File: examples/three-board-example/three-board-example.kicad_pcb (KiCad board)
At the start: 6 copper layers, 55 x 50 mm, 3 parts, among them U1 LM555xM, U2 LM555xM

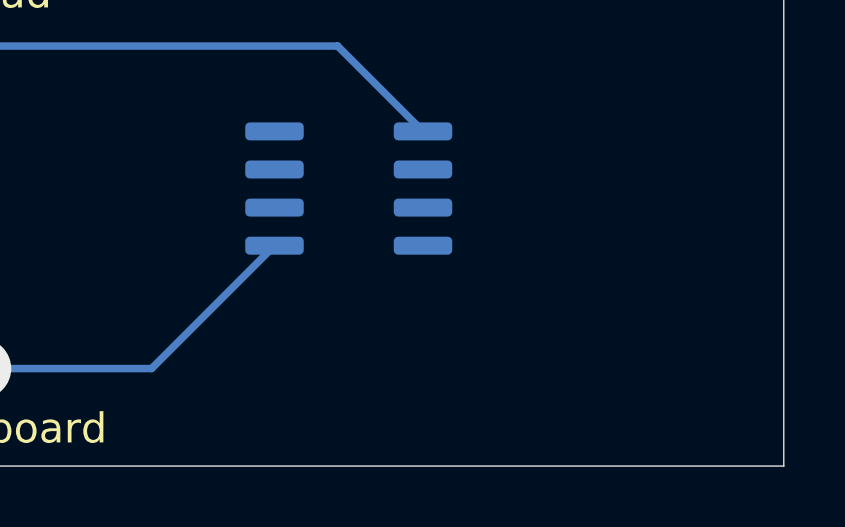
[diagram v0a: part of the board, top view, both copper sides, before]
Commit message: tracks working, and buried vias working
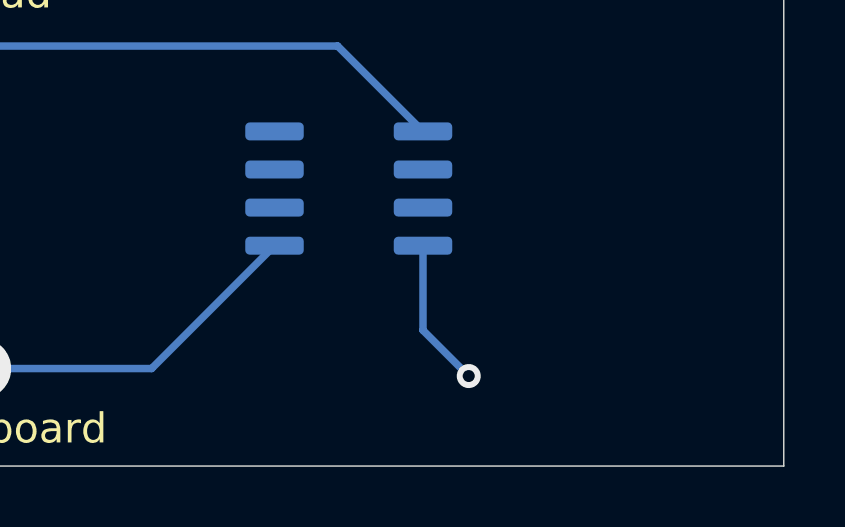
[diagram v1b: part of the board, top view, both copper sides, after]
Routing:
- net Net-(U2-Pad8): track 0.00 -> 9.73 mm, vias 0 -> 1

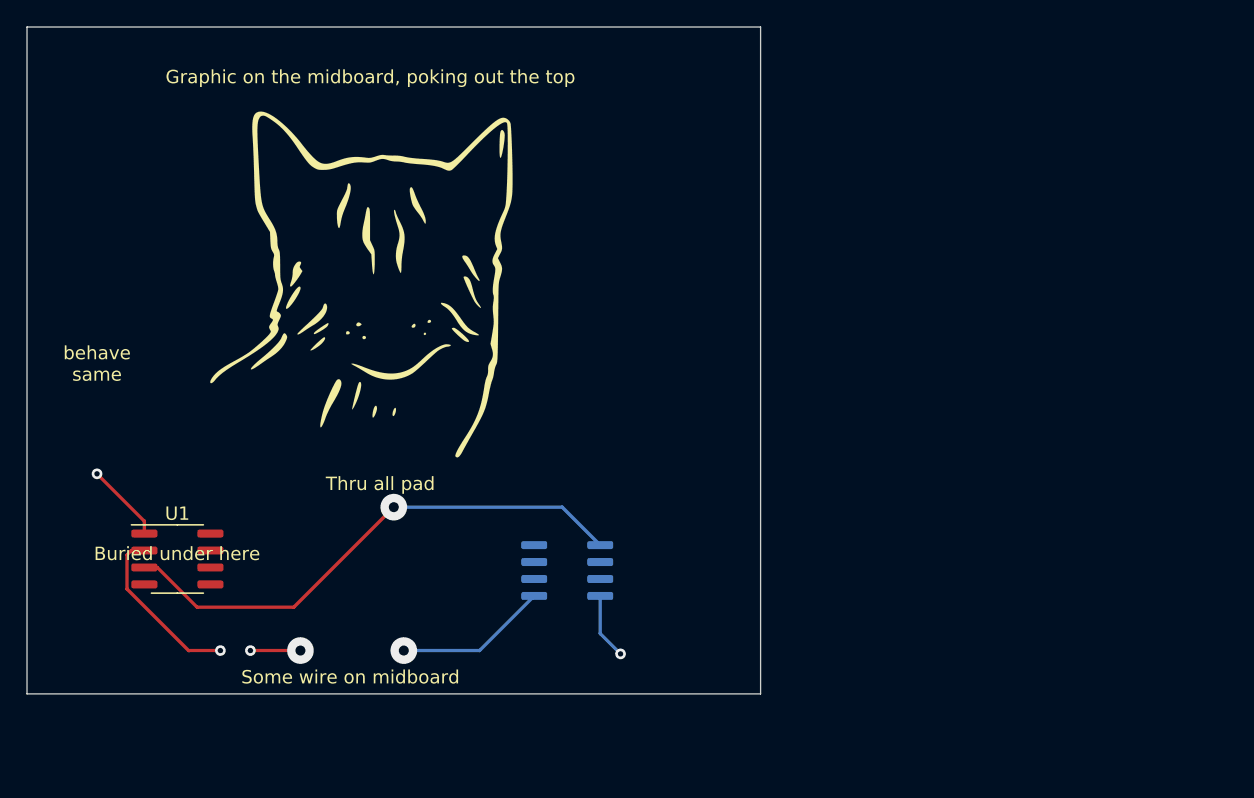
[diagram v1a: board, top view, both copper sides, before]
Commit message: vias and bond pads working. checked with inside and outside styles
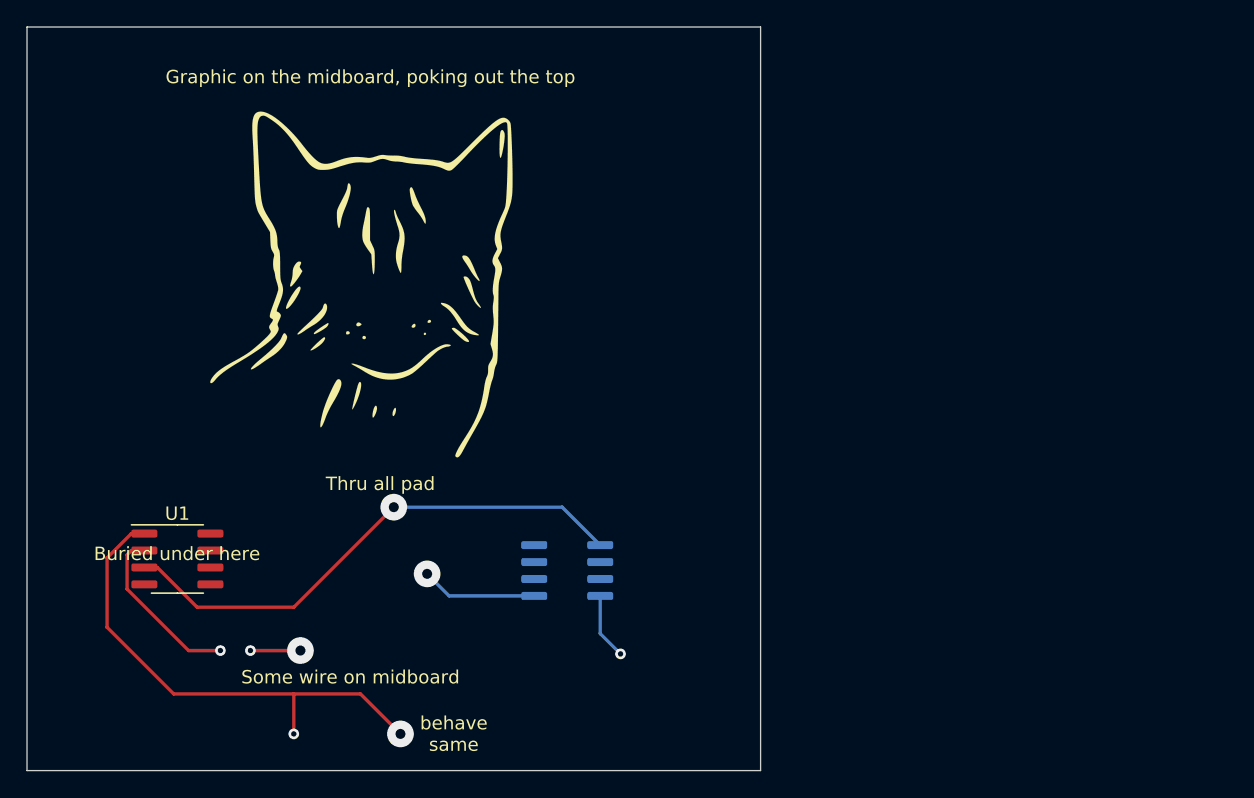
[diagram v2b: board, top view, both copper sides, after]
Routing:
- net Net-(U1-Pad1): track 14.5 -> 49.1 mm, vias 2 -> 4
- net Net-(U1-Pad2): track 38.1 -> 40.7 mm
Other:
- board size 55 x 50 mm -> 55 x 55.8 mm

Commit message: Special modules for cutting, meaning that the drawings from within the modules are exploded to cut layers
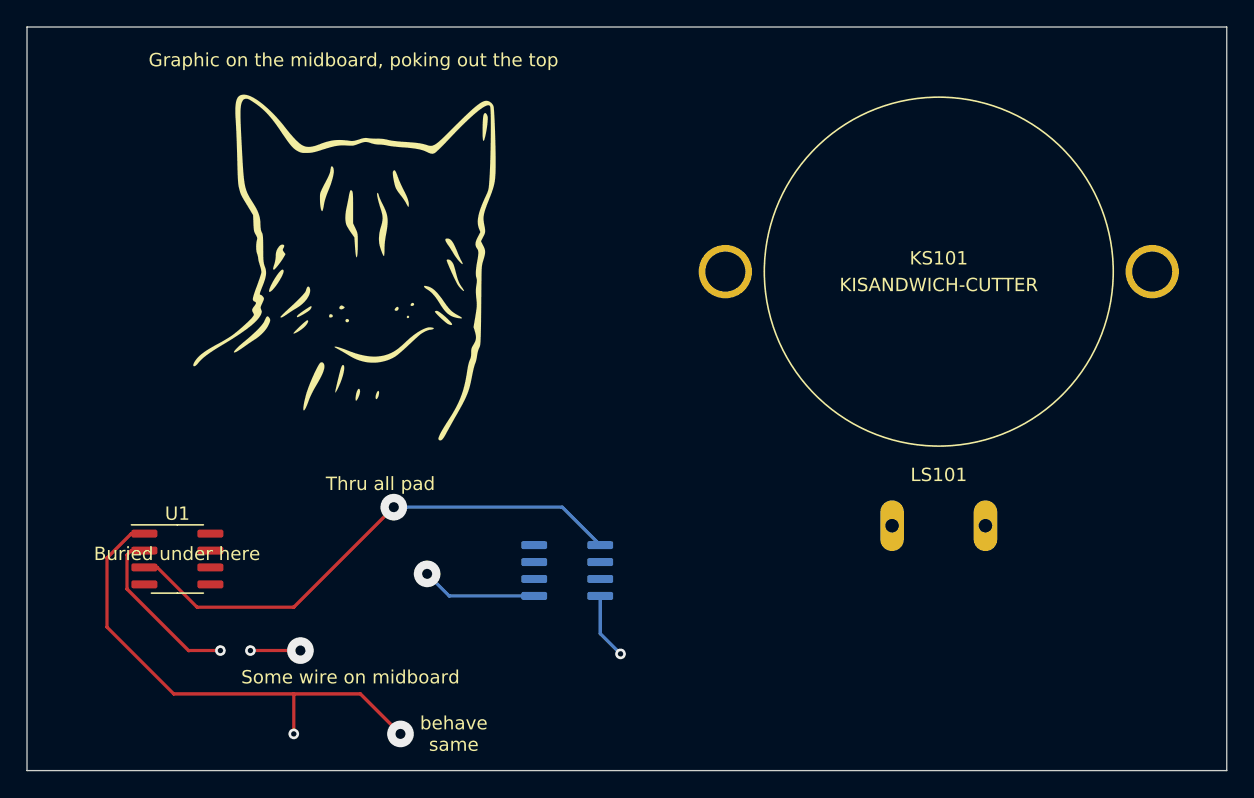
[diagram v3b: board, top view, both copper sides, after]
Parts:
- added KS101: KISANDWICH-CUTTER, Alex_Connectors:CUI-speaker-3layer-tight, F.Cu at (213.4, 53.3)
- added LS101: Speaker, Alex_Connectors:Speaker_CUI_CLS0281MAE_embedded, F.Cu at (213.4, 53.3)
- moved G1 1.80 mm to (168.7, 53.0)
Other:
- board size 55 x 55.8 mm -> 89.9 x 55.8 mm

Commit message: Made 3D representations. Changed speaker to being placed on midboard. Checked heights
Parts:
- LS101: value Speaker -> KISANDWICH-MIDBOARD
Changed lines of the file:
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@@
     (add_net "Net-(U2-Pad8)")
-  )
-  (module Alex_Connectors:Speaker_CUI_CLS0281MAE_embedded (layer F.Cu)
-    (at 213.36 53.34 180)
-    (fp_text reference LS101 (at 0 -15.24) (layer F.SilkS)
-      (effects (font (size 1 1) (thickness 0.15)))
-    )
-    (fp_text value Speaker (at 0 15.24) (layer F.Fab)
-      (effects (font (size 1 1) (thickness 0.15)))
-    )
-    (fp_arc (start -17.018 0) (end -18.414999 -1.333499) (angle -88.7) (layer B.SilkS) (width 0.12))
-    (fp_arc (start 17.018 0) (end 18.414999 1.333499) (angle -88.7) (layer B.SilkS) (width 0.12))
-    (fp_arc (start 17.018 0) (end 18.414999 1.333499) (angle -88.66778015) (layer B.CrtYd) (width 0.12))
-    (fp_arc (start -17.018 0) (end -18.414999 -1.333499) (angle -88.66778015) (layer B.CrtYd) (width 0.12))
-    (fp_circle (center 0 0) (end 13.97 0) (layer F.CrtYd) (width 0.12))
-    (fp_line (start -18.415 -1.3335) (end -9.3345 -10.4775) (layer B.SilkS) (width 0.12))
-    (fp_line (start 18.415 1.3335) (end 9.3345 10.4775) (layer B.SilkS) (width 0.12))
-    (fp_line (start -18.383618 1.365618) (end -9.271 10.541) (layer B.SilkS) (width 0.12))
-    (fp_circle (center 0 0) (end 14.00048 0) (layer B.SilkS) (width 0.12))
-    (fp_line (start 18.383618 -1.365618) (end 9.271 -10.541) (layer B.SilkS) (width 0.12))
-    (fp_circle (center 0 0) (end 13.081 0) (layer F.SilkS) (width 0.12))
-    (fp_line (start 18.415 1.3335) (end 9.3345 10.4775) (layer B.CrtYd) (width 0.12))
-    (fp_line (start 18.383618 -1.365618) (end 9.271 -10.541) (layer B.CrtYd) (width 0.12))
-    (fp_line (start -18.383618 1.365618) (end -9.271 10.541) (layer B.CrtYd) (width 0.12))
-    (fp_line (start -18.415 -1.3335) (end -9.3345 -10.4775) (layer B.CrtYd) (width 0.12))
-    (fp_circle (center 0 0) (end 12.954 0) (layer Dwgs.User) (width 0.12))
-    (fp_circle (center 0 0) (end 14.00048 0) (layer B.CrtYd) (width 0.12))
-    (pad 1 thru_hole oval (at -3.50012 -19.05 270) (size 3.81 1.778) (drill 1.016) (layers *.Cu *.Mask)
-      (net 15 "Net-(LS101-Pad1)"))
-    (pad 2 thru_hole oval (at 3.50012 -19.05 270) (size 3.81 1.778) (drill 1.016) (layers *.Cu *.Mask)
-      (net 16 "Net-(LS101-Pad2)"))
-    (pad "" thru_hole circle (at 16.002 0 180) (size 4 4) (drill 2.999999) (layers *.Cu *.Mask))
-    (pad "" thru_hole circle (at -16.002 0 180) (size 4 4) (drill 2.999999) (layers *.Cu *.Mask))
-    (model ${ATAIT_3D_DIR}/CUI_DEVICES_CLS0281MAE-L152.step
-      (offset (xyz 0 0 1.3))
-      (scale (xyz 1 1 1))
-      (rotate (xyz 90 0 0))
-    )
   )
   (module Alex_Connectors:CUI-speaker-3layer-tight (layer F.Cu)
@@
     (fp_arc (start 11.723 -16.204) (end 8.723 -16.204) (angle -54.117) (layer Eco2.User) (width 0.1))
     (fp_arc (start 0 0) (end -8.624 -11.029) (angle -283.955) (layer Margin) (width 0.1))
+    (fp_line (start -18.32 -1.408) (end -9.941 -9.858) (layer Eco1.User) (width 0.1))
+    (fp_line (start -18.32 1.408) (end -9.941 9.858) (layer Eco1.User) (width 0.1))
+    (fp_line (start 18.32 1.408) (end 9.941 9.858) (layer Eco1.User) (width 0.1))
+    (fp_line (start 18.32 -1.408) (end 9.941 -9.858) (layer Eco1.User) (width 0.1))
+    (fp_line (start -7.746 -4.472) (end -11.843 -6.837) (layer Eco2.User) (width 0.1))
+    (fp_line (start 7.746 -4.472) (end 11.843 -6.837) (layer Eco2.User) (width 0.1))
+    (fp_line (start -8.723 -16.204) (end -8.723 -19.425) (layer Eco2.User) (width 0.1))
+    (fp_line (start 8.723 -16.204) (end 8.723 -19.425) (layer Eco2.User) (width 0.1))
+    (fp_line (start -6.723 -21.425) (end 6.723 -21.425) (layer Eco2.User) (width 0.1))
+    (fp_line (start -8.624 -18.88) (end -8.624 -11.029) (layer Margin) (width 0.1))
+    (fp_line (start 8.624 -18.88) (end 8.624 -11.029) (layer Margin) (width 0.1))
     (fp_line (start -8.624 -18.88) (end 8.624 -18.88) (layer Margin) (width 0.1))
-    (fp_line (start 8.624 -18.88) (end 8.624 -11.029) (layer Margin) (width 0.1))
-    (fp_line (start -8.624 -18.88) (end -8.624 -11.029) (layer Margin) (width 0.1))
-    (fp_line (start -6.723 -21.425) (end 6.723 -21.425) (layer Eco2.User) (width 0.1))
-    (fp_line (start 8.723 -16.204) (end 8.723 -19.425) (layer Eco2.User) (width 0.1))
-    (fp_line (start -8.723 -16.204) (end -8.723 -19.425) (layer Eco2.User) (width 0.1))
-    (fp_line (start 7.746 -4.472) (end 11.843 -6.837) (layer Eco2.User) (width 0.1))
-    (fp_line (start -7.746 -4.472) (end -11.843 -6.837) (layer Eco2.User) (width 0.1))
-    (fp_line (start 18.32 -1.408) (end 9.941 -9.858) (layer Eco1.User) (width 0.1))
-    (fp_line (start 18.32 1.408) (end 9.941 9.858) (layer Eco1.User) (width 0.1))
-    (fp_line (start -18.32 1.408) (end -9.941 9.858) (layer Eco1.User) (width 0.1))
-    (fp_line (start -18.32 -1.408) (end -9.941 -9.858) (layer Eco1.User) (width 0.1))
+  )
+  (module Alex_Connectors:Speaker_CUI_CLS0281MAE_embedded (layer F.Cu)
+    (at 213.36 53.34 180)
+    (fp_text reference LS101 (at 0 -15.24) (layer F.SilkS)
+      (effects (font (size 1 1) (thickness 0.15)))
+    )
+    (fp_text value KISANDWICH-MIDBOARD (at 0 15.24) (layer F.Fab)
+      (effects (font (size 1 1) (thickness 0.15)))
+    )
+    (fp_circle (center 0 0) (end 13.97 0) (layer F.CrtYd) (width 0.12))
+    (fp_line (start -18.415 -1.3335) (end -9.3345 -10.4775) (layer B.SilkS) (width 0.12))
+    (fp_line (start 18.415 1.3335) (end 9.3345 10.4775) (layer B.SilkS) (width 0.12))
+    (fp_line (start -18.383618 1.365618) (end -9.271 10.541) (layer B.SilkS) (width 0.12))
+    (fp_circle (center 0 0) (end 14.00048 0) (layer B.SilkS) (width 0.12))
+    (fp_line (start 18.383618 -1.365618) (end 9.271 -10.541) (layer B.SilkS) (width 0.12))
+    (fp_circle (center 0 0) (end 13.081 0) (layer F.SilkS) (width 0.12))
+    (fp_line (start 18.415 1.3335) (end 9.3345 10.4775) (layer B.CrtYd) (width 0.12))
+    (fp_line (start 18.383618 -1.365618) (end 9.271 -10.541) (layer B.CrtYd) (width 0.12))
+    (fp_line (start -18.383618 1.365618) (end -9.271 10.541) (layer B.CrtYd) (width 0.12))
+    (fp_line (start -18.415 -1.3335) (end -9.3345 -10.4775) (layer B.CrtYd) (width 0.12))
+    (fp_circle (center 0 0) (end 12.954 0) (layer Dwgs.User) (width 0.12))
+    (fp_circle (center 0 0) (end 14.00048 0) (layer B.CrtYd) (width 0.12))
+    (fp_arc (start -17.018 0) (end -18.414999 -1.333499) (angle -88.7) (layer B.SilkS) (width 0.12))
+    (fp_arc (start 17.018 0) (end 18.414999 1.333499) (angle -88.7) (layer B.SilkS) (width 0.12))
+    (fp_arc (start 17.018 0) (end 18.414999 1.333499) (angle -88.66778015) (layer B.CrtYd) (width 0.12))
+    (fp_arc (start -17.018 0) (end -18.414999 -1.333499) (angle -88.66778015) (layer B.CrtYd) (width 0.12))
+    (pad 1 thru_hole oval (at -3.50012 -19.05 270) (size 3.81 1.778) (drill 1.016) (layers *.Cu *.Mask)
+      (net 15 "Net-(LS101-Pad1)"))
+    (pad 2 thru_hole oval (at 3.50012 -19.05 270) (size 3.81 1.778) (drill 1.016) (layers *.Cu *.Mask)
+      (net 16 "Net-(LS101-Pad2)"))
+    (pad "" thru_hole circle (at 16.002 0 180) (size 4 4) (drill 2.999999) (layers *.Cu *.Mask))
+    (pad "" thru_hole circle (at -16.002 0 180) (size 4 4) (drill 2.999999) (layers *.Cu *.Mask))
     (model ${ATAIT_3D_DIR}/CUI_DEVICES_CLS0281MAE-L152.step
-      (at (xyz 0 0 0))
+      (offset (xyz 0 0 1.3))
       (scale (xyz 1 1 1))
       (rotate (xyz 90 0 0))

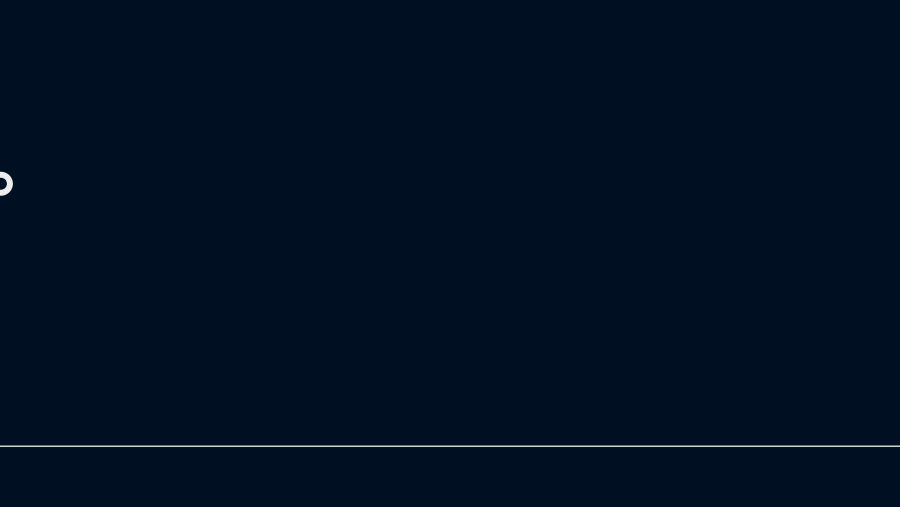
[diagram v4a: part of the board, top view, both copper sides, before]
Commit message: Also processing copper that is in cutter modules
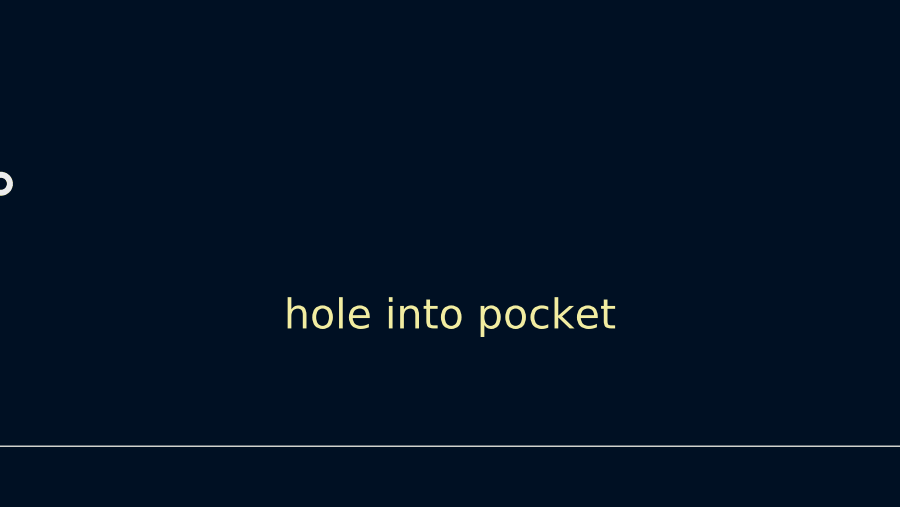
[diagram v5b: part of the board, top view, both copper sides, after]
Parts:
- added svg2mod: KISANDWICH-CUTTER, Alex_Sandwiches:light-hole, F.Cu at (201.9, 77.5)
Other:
- board text added: "hole into pocket"
